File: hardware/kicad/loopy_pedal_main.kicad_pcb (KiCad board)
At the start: 2 copper layers, 100 x 98 mm, 88 parts, among them J1 USB_C_Receptacle_USB2.0_16P, J10 Conn_01x02, J2 Barrel_Jack, J3 Conn_01x06, J4 Conn_01x06, J5 Conn_01x08, J6 Conn_02x03_Odd_Even, J7 Conn_02x03_Odd_Even, J8 DIN-5_180degree, J9 DIN-5_180degree, Q1 AO3401A, SW1 SW_Push, SW2 SW_Push, U1 ATmega328P-A, U10 74AHCT1G08, U2 ATmega16U2-A, U3 AP63203WU, U4 74AHCT1G125, U5 LM66100DCK, U6 LM66100DCK, U7 USBLC6-2SC6, U8 74AHCT1G125, U9 H11L1, Y1 16MHz, Y2 16MHz

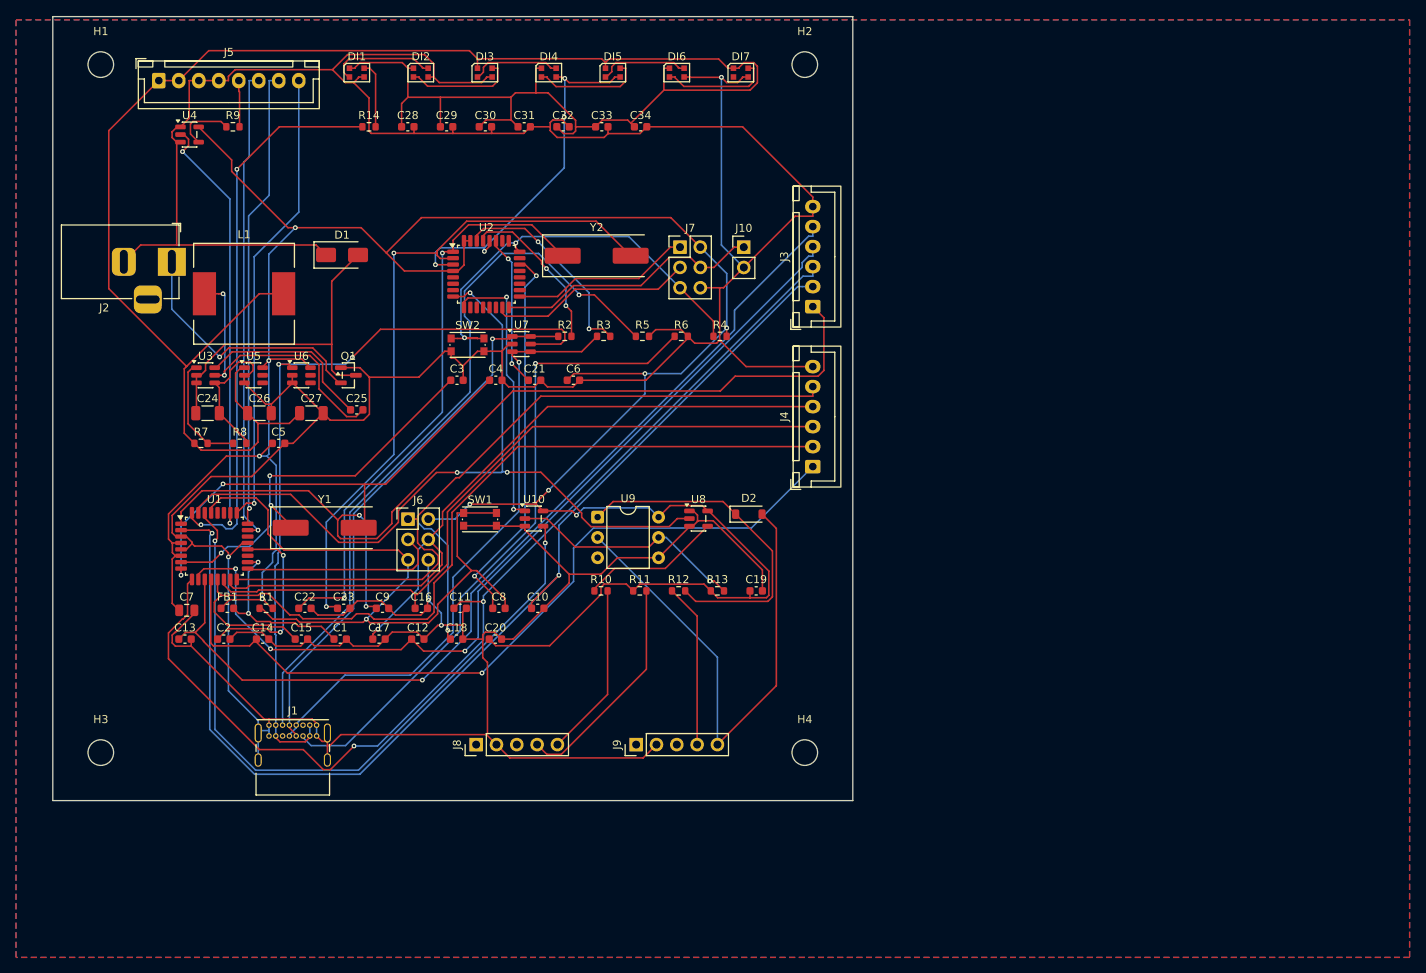
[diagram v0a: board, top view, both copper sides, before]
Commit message: feat(pcb): real DIN-5 MIDI jacks, off-board indicator LEDs, all I/O on bottom
Reworks the main board per review feedback:
- Indicator LEDs leave the board: the 7 on-board WS2812Bs are replaced by a
  3-pin breakout header (J11: +5V_LED / data / GND); only the 330R series
  resistor + decoupling stay. They now live on a separate off-board strip.
- J8/J9 are real 5-pin DIN MIDI sockets (new loopy:MIDI_DIN5_SDS-50J footprint,
  CUI SDS-50J / Jalco YKF51 pattern, hand-built since KiCad has none).
- All external I/O (9V barrel, USB-C, both MIDI DIN) now on the bottom edge;
  footswitch headers moved to the left edge, ring/indicator to the top.
- 3D render fix: L1 and the ring WS2812Bs were invisible (KiCad ships those
  footprints without .step files); remapped to existing models (Bourns SRR1260;
  WS2812B-Mini scaled to 2.0mm).

Rebuilt from netlist + re-placed + re-routed: 100x98mm, 72 parts,
984 segments / 86 vias, 0 DRC errors / 0 unrouted. Gerbers + doc updated.

Co-Authored-By: Claude Opus 4.8 <noreply@anthropic.com>
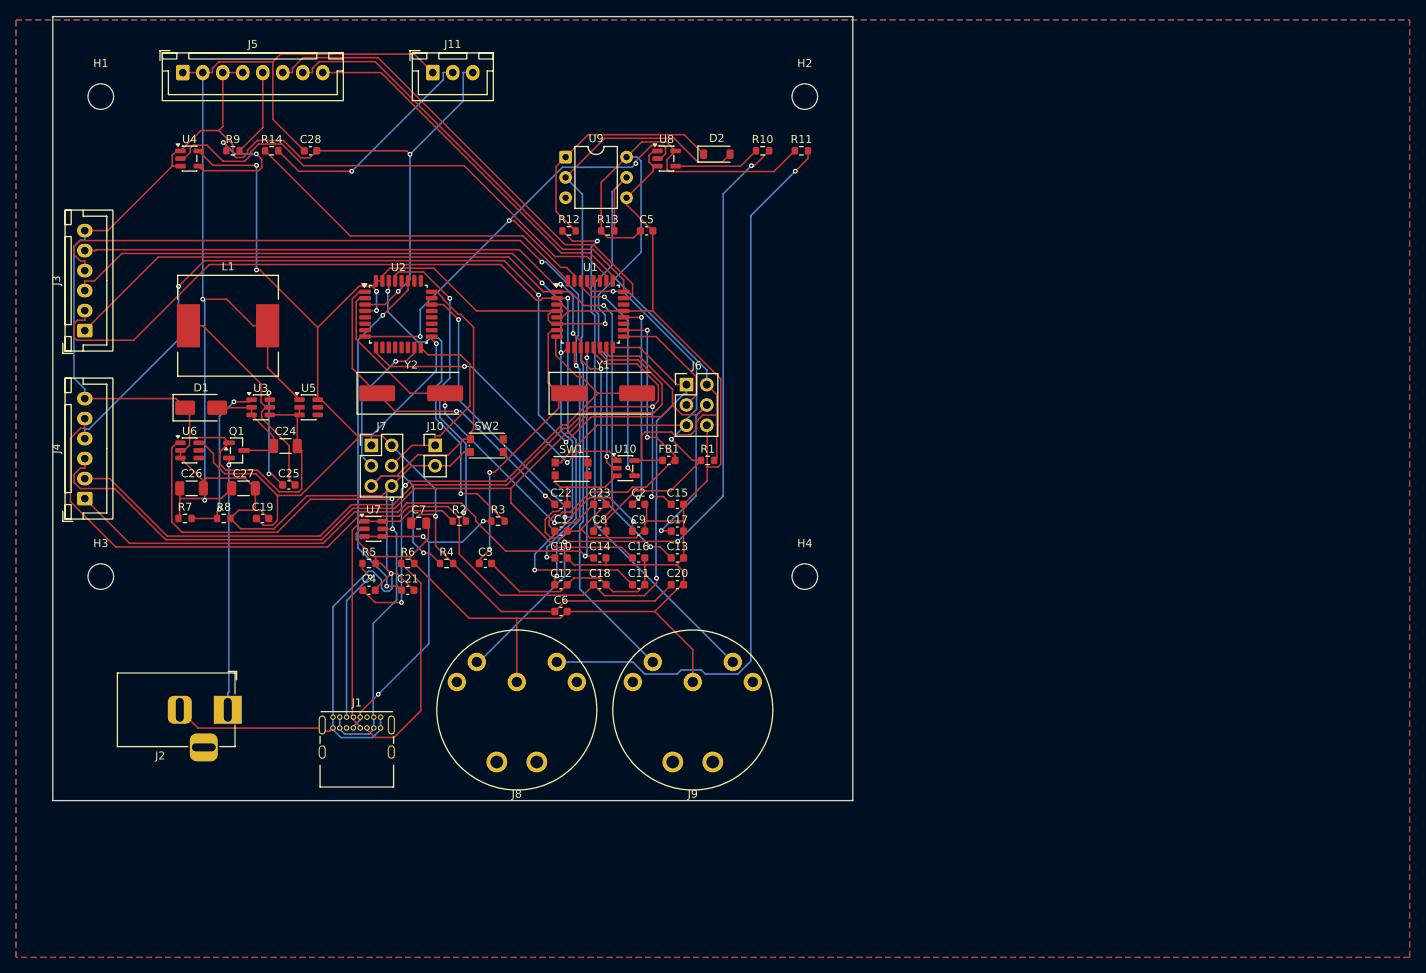
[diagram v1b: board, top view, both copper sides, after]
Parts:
- removed C29, C30, C31, C32, C33, C34: 100nF, Capacitor_SMD:C_0603_1608Metric
- removed DI1, DI2, DI3, DI4, DI5, DI6, DI7: WS2812B, LED_SMD:LED_WS2812B-2020_PLCC4_2.0x2.0mm
- added J11: Conn_01x03, JST_XH_B3B-XH-A_1x03_P2.50mm_Vertical, F.Cu at (77.5, 37.0)
- C1, C10, C11, C12, C13, C14, C15, C16, C17, C18, C19, C2, C20, C21, C22, C23, C25, C28, C3, C4, C5, C6, C8, C9: footprint Capacitor_SMD:C_0603_1608Metric -> C_0603_1608Metric
- C24, C26, C27: footprint Capacitor_SMD:C_1206_3216Metric -> C_1206_3216Metric
- C7: footprint Capacitor_SMD:C_0805_2012Metric -> C_0805_2012Metric
- D1: footprint Diode_SMD:D_SMA -> D_SMA
- D2: footprint Diode_SMD:D_SOD-123 -> D_SOD-123
- FB1: footprint Inductor_SMD:L_0603_1608Metric -> L_0603_1608Metric
- J1: footprint Connector_USB:USB_C_Receptacle_GCT_USB4085 -> USB_C_Receptacle_GCT_USB4085
- J10: footprint Connector_PinHeader_2.54mm:PinHeader_1x02_P2.54mm_Vertical -> PinHeader_1x02_P2.54mm_Vertical
- J2: footprint Connector_BarrelJack:BarrelJack_Horizontal -> BarrelJack_Horizontal
- J3, J4: footprint Connector_JST:JST_XH_B6B-XH-A_1x06_P2.50mm_Vertical -> JST_XH_B6B-XH-A_1x06_P2.50mm_Vertical
- J5: footprint Connector_JST:JST_XH_B8B-XH-A_1x08_P2.50mm_Vertical -> JST_XH_B8B-XH-A_1x08_P2.50mm_Vertical
- J6, J7: footprint Connector_PinHeader_2.54mm:PinHeader_2x03_P2.54mm_Vertical -> PinHeader_2x03_P2.54mm_Vertical
- J8, J9: footprint Connector_PinHeader_2.54mm:PinHeader_1x05_P2.54mm_Vertical -> MIDI_DIN5_SDS-50J
- L1: footprint Inductor_SMD:L_12x12mm_H8mm -> L_12x12mm_H8mm
- Q1: footprint Package_TO_SOT_SMD:SOT-23 -> SOT-23
- R1, R10, R11, R12, R13, R14, R2, R3, R4, R5, R6, R7, R8, R9: footprint Resistor_SMD:R_0603_1608Metric -> R_0603_1608Metric
- SW1, SW2: footprint Button_Switch_SMD:SW_Push_1P1T_NO_CK_KMR2 -> SW_Push_1P1T_NO_CK_KMR2
- U1, U2: footprint Package_QFP:TQFP-32_7x7mm_P0.8mm -> TQFP-32_7x7mm_P0.8mm
- U10, U4, U8: footprint Package_TO_SOT_SMD:SOT-23-5 -> SOT-23-5
- U3, U5, U6, U7: footprint Package_TO_SOT_SMD:SOT-23-6 -> SOT-23-6
- U9: footprint Package_DIP:DIP-6_W7.62mm -> DIP-6_W7.62mm
- Y1, Y2: footprint Crystal:Crystal_SMD_HC49-SD -> Crystal_SMD_HC49-SD
- moved J4 91.1 mm to (34.0, 90.2)
- moved J3 91.0 mm to (34.0, 69.2)
- moved C13 62.4 mm to (108.1, 97.7)
- moved C19 62.4 mm to (56.2, 92.7)
- moved R11 58.6 mm to (123.6, 46.8)
- moved R10 58.6 mm to (118.7, 46.8)
- moved R1 58.2 mm to (111.9, 85.5)
- moved FB1 58.2 mm to (107.0, 85.5)
- moved J2 56.4 mm to (51.9, 116.7)
- moved U1 55.2 mm to (97.2, 67.2)
- moved C2 54.5 mm to (103.2, 91.0)
- moved C5 53.1 mm to (104.2, 56.8)
- moved C15 49.9 mm to (108.1, 91.0)
- moved R12 47.0 mm to (94.5, 56.8)
- moved R13 47.0 mm to (99.4, 56.8)
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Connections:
- R14 pad 2: IND_D0 -> IND_DATA_OUT
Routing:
- net GND: track 698.5 -> 553.3 mm, vias 8 -> 3
- net +5V_LED: track 264.6 -> 131.2 mm, vias 0 -> 2
- net N$14: track 92.0 -> 20.8 mm
- net N$17: track 21.8 -> 87.7 mm, vias 0 -> 3
- net N$18: track 28.4 -> 92.7 mm, vias 0 -> 1
- net UART_RX: track 88.2 -> 28.1 mm
- net N$15: track 82.3 -> 28.1 mm, vias 1 -> 0
- net N$19: track 20.5 -> 65.1 mm, vias 0 -> 1
- net SW_CLEAR: track 103.7 -> 144.8 mm, vias 1 -> 4
- net N$8: track 84.9 -> 47.6 mm
- net UART_TX: track 99.7 -> 63.4 mm
- net SW_STOP: track 140.8 -> 107.6 mm
- net +5V: track 334.2 -> 301.7 mm, vias 9 -> 6
- net USB_D-: track 76.4 -> 44.4 mm, vias 1 -> 3
- net SW_TRACK4: track 89.2 -> 119.8 mm
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
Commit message: fix(pcb): edge-mount connectors, fix barrel orientation, model + show DIN jacks
Addresses render feedback on the main board:
- Barrel jack rotation was wrong (opening faced into the board); now rot 90 so
  the 9V opening faces out the bottom edge.
- All bottom-edge external connectors (barrel, USB-C, both MIDI DIN) are now
  aligned to the board boundary with a ~1.5-2mm overhang via a new edge-align
  placement helper, so the ports are reachable from outside instead of sitting
  inset.
- The DIN-5 jacks now have a 3D body: MIDI_DIN5.scad -> OpenSCAD -> STL ->
  MIDI_DIN5.wrl, attached at scale 0.3937 (cancels KiCad's wrl unit factor) so
  they render as round sockets facing the edge.
- Tightened the layout: 100x92mm (was 100x98), less dead space; gave the opto
  (U9, DIP) its own room so the route comes back clean.

Re-routed: 938 segments / 80 vias, 0 DRC errors / 0 unrouted. Gerbers + doc updated.

Co-Authored-By: Claude Opus 4.8 <noreply@anthropic.com>
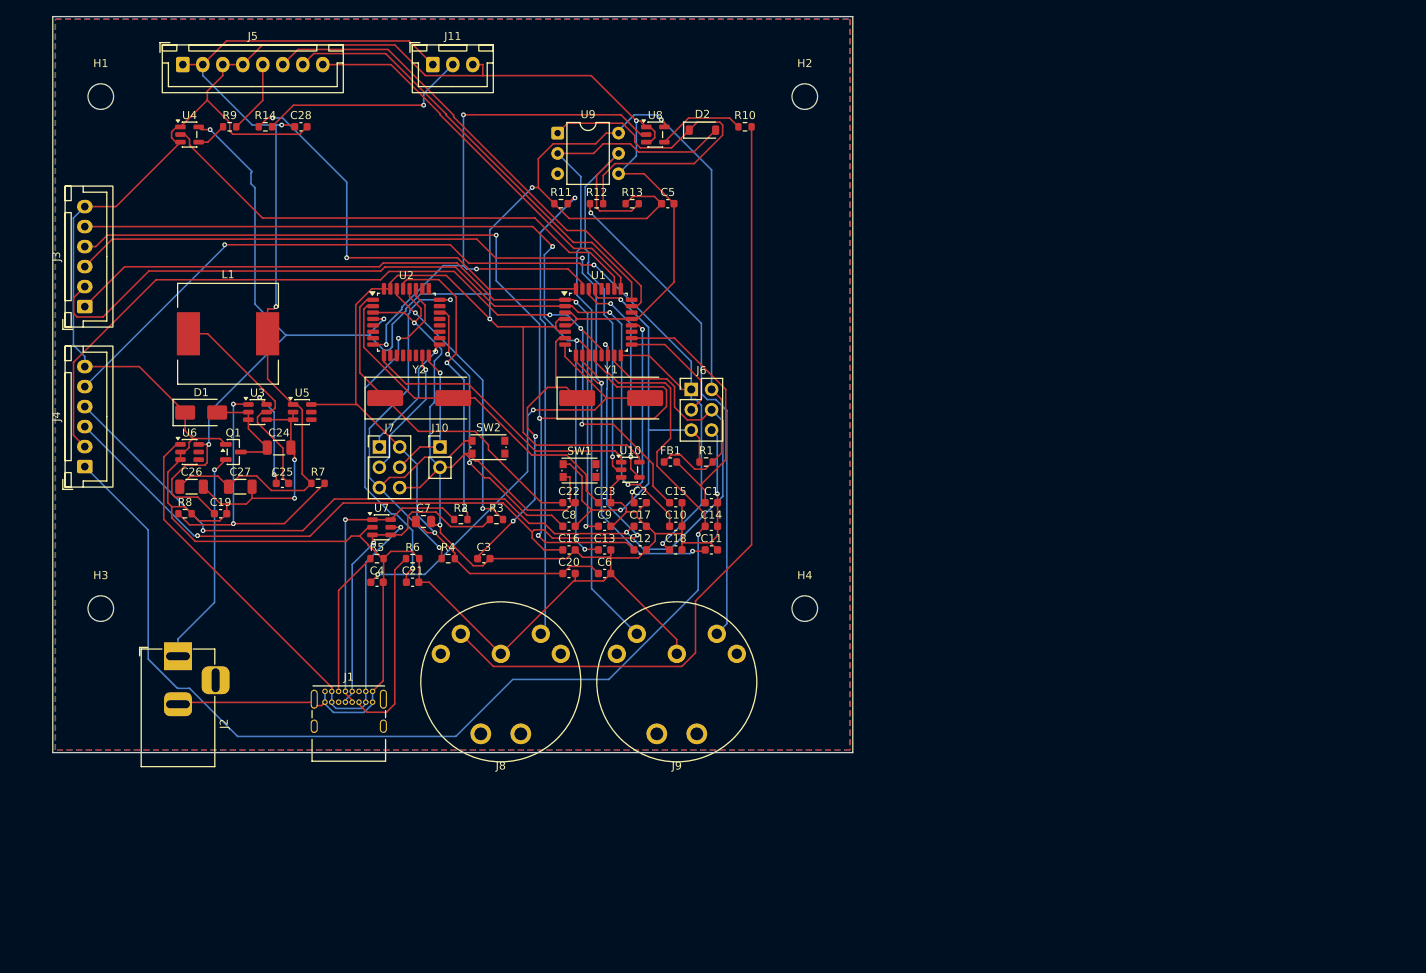
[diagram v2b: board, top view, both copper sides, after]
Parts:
- moved R11 30.8 mm to (93.5, 53.4)
- moved C1 19.1 mm to (112.3, 90.8)
- moved R7 17.2 mm to (63.2, 88.3)
- moved C10 14.9 mm to (107.9, 93.7)
- moved C14 14.5 mm to (112.3, 93.7)
- moved C20 13.6 mm to (94.5, 99.6)
- moved C12 10.8 mm to (103.4, 96.7)
- moved C18 10.4 mm to (107.9, 96.7)
- moved C11 10.1 mm to (112.3, 96.7)
- moved C13 9.15 mm to (99.0, 96.7)
- moved J2 9.14 mm to (45.6, 110.0), turned to 90 degrees
- moved C16 8.76 mm to (94.5, 96.7)
- moved C6 7.23 mm to (99.0, 99.6)
- moved C19 5.28 mm to (51.0, 92.1)
- moved R8 4.89 mm to (46.5, 92.1)
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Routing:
- net SW_TRACK2: track 97.3 -> 148.0 mm, vias 2 -> 1
- net +5V: track 301.7 -> 347.8 mm, vias 6 -> 7
- net N$18: track 92.7 -> 58.0 mm
- net SW_MODE: track 110.3 -> 136.1 mm
- net GND: track 553.3 -> 529.8 mm, vias 3 -> 6
- net SW_CLEAR: track 144.8 -> 124.3 mm, vias 4 -> 2
- net FB: track 21.0 -> 37.8 mm
- net N$20: track 30.2 -> 46.2 mm
- net +5V_LED: track 131.2 -> 116.7 mm
- net UART_TX: track 63.4 -> 76.2 mm
- net N$17: track 87.7 -> 100.4 mm, vias 3 -> 0
- net RING_DATA_BUF: track 16.2 -> 3.85 mm, vias 2 -> 0
- net RST_328: track 68.6 -> 57.5 mm
- net MIDI_IN_OPTO: track 46.6 -> 57.3 mm
- net DTR: track 46.3 -> 35.8 mm
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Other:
- board size 100 x 98 mm -> 100 x 92 mm
